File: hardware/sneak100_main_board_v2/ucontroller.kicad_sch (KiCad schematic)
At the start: 26 parts, among them SW1 SW_Push, U1 STM32F405RGTx, Y1 8MHz

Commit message: PCB version 2.0 schematic progress
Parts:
- removed JP1, JP2: (no value), symbol Jumper:SolderJumper_3_Open
- added R3, R6: (no value), symbol Device:R
- added SW1: (no value), symbol Switch:SW_DIP_x04
- C10: renamed from C9; value (none) -> 100nF
- C11: renamed from C10; value (none) -> 100nF
- C12: renamed from C11; value (none) -> 4.7uF
- C5: renamed from C12; value (none) -> 100nF
- C6: renamed from C2; value (none) -> 100nF
- C7: renamed from C5; value (none) -> 1uF
- C8: renamed from C7; value (none) -> 100nF
- C9: renamed from C8; value (none) -> 100nF
- J1: value (none) -> USB_B_Mini
- J2: value (none) -> Conn_02x05_Odd_Even
- J3: value (none) -> Conn_01x03
- L1: value (none) -> 4.7uH
- R1, R2: value (none) -> 22
- R7: renamed from R3; value (none) -> 10k
- renumbered C4 to C1, C6 to C2, C1 to C3, C3 to C4, SW1 to SW2
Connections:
- net +3V3: now also R4.1, R5.1, R3.1, R6.1
- net BOOT0: now also R3.2, SW1.8; no longer R4.2
- net GND: now also SW1.1, SW1.2, SW1.3, SW1.4
- net SW1: now reaches U1.36 (PB15)
- net SW1: now also R4.2, SW1.7
- net SW2: now reaches U1.39 (PC8)
- net SW2: now also R5.2, SW1.6
- net SW3: now reaches U1.40 (PC9)
- net SW3: now also R6.2, SW1.5
- net BOOT1: no longer names the net of U1.28 (PB2)
- net BOOT1: no longer R5.2
- net IMU_INT: no longer names the net of U1.26 (PB0)
- no-connect marks 13 -> 12
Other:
- note added: "boot region selection and user switches"
- note removed: "boot region selection"
- moved on the sheet: C1, C10, C11, C12, C2, C3, C4, C5, C6, C7, C8, C9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

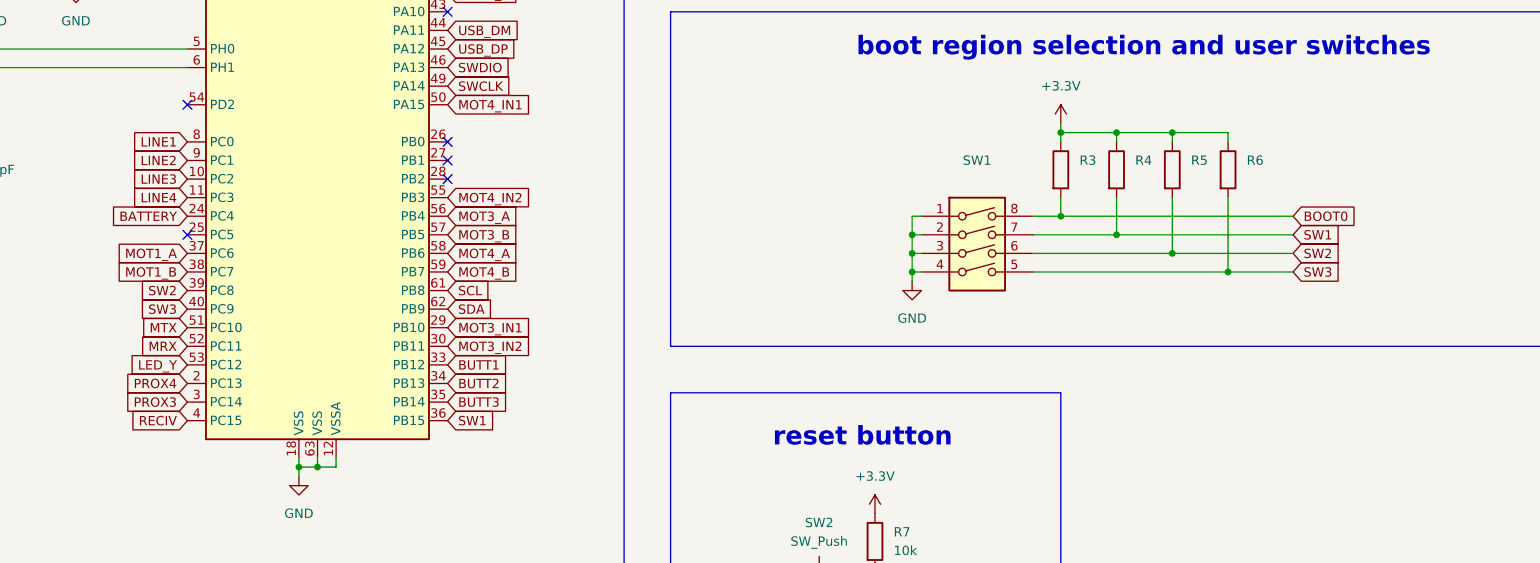
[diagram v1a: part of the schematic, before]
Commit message: include BOOT1 switch into new PCB
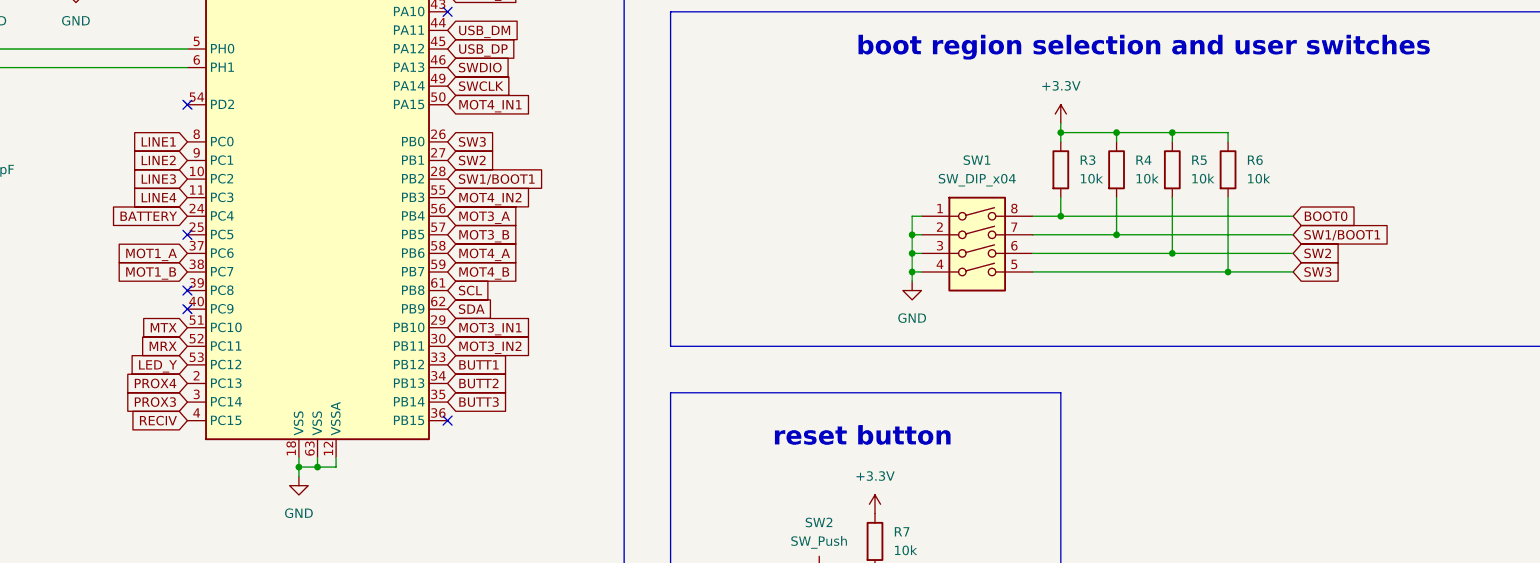
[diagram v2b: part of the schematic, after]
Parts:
- R3, R4, R5, R6: value (none) -> 10k
- SW1: value (none) -> SW_DIP_x04
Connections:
- net SW2: now also U1.27 (PB1); no longer U1.39 (PC8)
- net SW3: now also U1.26 (PB0); no longer U1.40 (PC9)
- net SW1/BOOT1: now reaches U1.28 (PB2)
- net SW1/BOOT1: now also R4.2, SW1.7
- removed net SW1: R4.2, SW1.7, U1.36 (PB15)
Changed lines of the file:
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@@
   (no_connect (at 236.22 50.8))
   (no_connect (at 83.82 99.06))
-  (no_connect (at 119.38 88.9))
   (no_connect (at 119.38 68.58))
   (no_connect (at 172.72 39.37))
   (no_connect (at 185.42 44.45))
   (no_connect (at 172.72 44.45))
+  (no_connect (at 119.38 124.46))
   (no_connect (at 246.38 45.72))
-  (no_connect (at 119.38 86.36))
   (no_connect (at 246.38 35.56))
-  (no_connect (at 119.38 91.44))
+  (no_connect (at 83.82 109.22))
+  (no_connect (at 83.82 106.68))
   (no_connect (at 83.82 81.28))
   (polyline (pts (xy 203.2 120.65) (xy 203.2 163.83))
@@
     )
   )
-  (global_label "SW1" (shape input) (at 119.38 124.46 0) (fields_autoplaced)
-    (effects (font (size 1.27 1.27)) (justify left))
-    (property "Intersheet References" "${INTERSHEET_REFS}" (id 0) (at 125.6636 124.3806 0)
+  (global_label "SW1{slash}BOOT1" (shape input) (at 119.38 91.44 0) (fields_autoplaced)
+    (effects (font (size 1.27 1.27)) (justify left))
+    (property "Intersheet References" "${INTERSHEET_REFS}" (id 0) (at 133.1021 91.3606 0)
       (effects (font (size 1.27 1.27)) (justify left) hide)
     )
@@
     )
   )
-  (global_label "SW2" (shape input) (at 83.82 106.68 180) (fields_autoplaced)
-    (effects (font (size 1.27 1.27)) (justify right))
-    (property "Intersheet References" "${INTERSHEET_REFS}" (id 0) (at 77.5364 106.6006 0)
-      (effects (font (size 1.27 1.27)) (justify right) hide)
+  (global_label "SW2" (shape input) (at 119.38 88.9 0) (fields_autoplaced)
+    (effects (font (size 1.27 1.27)) (justify left))
+    (property "Intersheet References" "${INTERSHEET_REFS}" (id 0) (at 125.6636 88.9794 0)
+      (effects (font (size 1.27 1.27)) (justify left) hide)
     )
   )
@@
     )
   )
-  (global_label "SW1" (shape input) (at 234.95 99.06 0) (fields_autoplaced)
-    (effects (font (size 1.27 1.27)) (justify left))
-    (property "Intersheet References" "${INTERSHEET_REFS}" (id 0) (at 241.2336 98.9806 0)
+  (global_label "SW1{slash}BOOT1" (shape input) (at 234.95 99.06 0) (fields_autoplaced)
+    (effects (font (size 1.27 1.27)) (justify left))
+    (property "Intersheet References" "${INTERSHEET_REFS}" (id 0) (at 248.6721 98.9806 0)
       (effects (font (size 1.27 1.27)) (justify left) hide)
     )
@@
     )
   )
-  (global_label "SW3" (shape input) (at 83.82 109.22 180) (fields_autoplaced)
-    (effects (font (size 1.27 1.27)) (justify right))
-    (property "Intersheet References" "${INTERSHEET_REFS}" (id 0) (at 77.5364 109.1406 0)
-      (effects (font (size 1.27 1.27)) (justify right) hide)
+  (global_label "SW3" (shape input) (at 119.38 86.36 0) (fields_autoplaced)
+    (effects (font (size 1.27 1.27)) (justify left))
+    (property "Intersheet References" "${INTERSHEET_REFS}" (id 0) (at 125.6636 86.4394 0)
+      (effects (font (size 1.27 1.27)) (justify left) hide)
     )
   )
@@
       (effects (font (size 1.27 1.27)) (justify left))
     )
-    (property "Value" "" (id 1) (at 220.98 91.4399 0)
+    (property "Value" "10k" (id 1) (at 220.98 91.4399 0)
       (effects (font (size 1.27 1.27)) (justify left))
     )
@@
       (effects (font (size 1.27 1.27)) (justify left))
     )
-    (property "Value" "" (id 1) (at 205.74 91.4399 0)
+    (property "Value" "10k" (id 1) (at 205.74 91.4399 0)
       (effects (font (size 1.27 1.27)) (justify left))
     )
@@
       (effects (font (size 1.27 1.27)) (justify left))
     )
-    (property "Value" "" (id 1) (at 228.6 91.4399 0)
+    (property "Value" "10k" (id 1) (at 228.6 91.4399 0)
       (effects (font (size 1.27 1.27)) (justify left))
     )
@@
       (effects (font (size 1.27 1.27)) (justify left))
     )
-    (property "Value" "" (id 1) (at 213.36 91.4399 0)
+    (property "Value" "10k" (id 1) (at 213.36 91.4399 0)
       (effects (font (size 1.27 1.27)) (justify left))
     )
@@
     (in_bom yes) (on_board yes) (fields_autoplaced)
     (property "Reference" "SW1" (id 0) (at 191.77 88.9 0))
-    (property "Value" "" (id 1) (at 191.77 91.44 0))
+    (property "Value" "SW_DIP_x04" (id 1) (at 191.77 91.44 0))
     (property "Footprint" "" (id 2) (at 191.77 101.6 0)
       (effects (font (size 1.27 1.27)) hide)

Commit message: small improvements
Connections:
- net USB_5V: now reaches J1.1 (VBUS)
- net MRX renamed RX
- net MTX renamed TX
- no-connect marks 12 -> 11
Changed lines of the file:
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@@
   (no_connect (at 119.38 124.46))
   (no_connect (at 246.38 45.72))
-  (no_connect (at 246.38 35.56))
   (no_connect (at 83.82 109.22))
   (no_connect (at 83.82 106.68))
@@
     )
   )
-  (global_label "MTX" (shape input) (at 83.82 111.76 180) (fields_autoplaced)
-    (effects (font (size 1.27 1.27)) (justify right))
-    (property "Intersheet References" "${INTERSHEET_REFS}" (id 0) (at 77.7783 111.6806 0)
+  (global_label "TX" (shape input) (at 83.82 111.76 180) (fields_autoplaced)
+    (effects (font (size 1.27 1.27)) (justify right))
+    (property "Intersheet References" "${INTERSHEET_REFS}" (id 0) (at 79.2298 111.6806 0)
       (effects (font (size 1.27 1.27)) (justify right) hide)
     )
@@
     )
   )
-  (global_label "MRX" (shape input) (at 83.82 114.3 180) (fields_autoplaced)
-    (effects (font (size 1.27 1.27)) (justify right))
-    (property "Intersheet References" "${INTERSHEET_REFS}" (id 0) (at 77.4759 114.2206 0)
+  (global_label "RX" (shape input) (at 83.82 114.3 180) (fields_autoplaced)
+    (effects (font (size 1.27 1.27)) (justify right))
+    (property "Intersheet References" "${INTERSHEET_REFS}" (id 0) (at 78.9274 114.2206 0)
       (effects (font (size 1.27 1.27)) (justify right) hide)
     )
@@
     )
   )
-  (global_label "MRX" (shape input) (at 215.9 41.91 0) (fields_autoplaced)
-    (effects (font (size 1.27 1.27)) (justify left))
-    (property "Intersheet References" "${INTERSHEET_REFS}" (id 0) (at 222.2441 41.9894 0)
+  (global_label "RX" (shape input) (at 215.9 41.91 0) (fields_autoplaced)
+    (effects (font (size 1.27 1.27)) (justify left))
+    (property "Intersheet References" "${INTERSHEET_REFS}" (id 0) (at 220.7926 41.8306 0)
       (effects (font (size 1.27 1.27)) (justify left) hide)
     )
@@
     )
   )
-  (global_label "MTX" (shape input) (at 215.9 39.37 0) (fields_autoplaced)
-    (effects (font (size 1.27 1.27)) (justify left))
-    (property "Intersheet References" "${INTERSHEET_REFS}" (id 0) (at 221.9417 39.4494 0)
+  (global_label "TX" (shape input) (at 215.9 39.37 0) (fields_autoplaced)
+    (effects (font (size 1.27 1.27)) (justify left))
+    (property "Intersheet References" "${INTERSHEET_REFS}" (id 0) (at 220.4902 39.2906 0)
       (effects (font (size 1.27 1.27)) (justify left) hide)
     )
@@
       (effects (font (size 1.27 1.27)) (justify left) hide)
     )
+  )
+  (global_label "USB_5V" (shape input) (at 246.38 35.56 0) (fields_autoplaced)
+    (effects (font (size 1.27 1.27)) (justify left))
+    (property "Intersheet References" "${INTERSHEET_REFS}" (id 0) (at 255.8688 35.4806 0)
+      (effects (font (size 1.27 1.27)) (justify left) hide)
+    )
